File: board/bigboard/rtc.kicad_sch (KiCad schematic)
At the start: 4 parts, among them U12 PCF85263AT{slash}AJ, Y2 32.768kHz

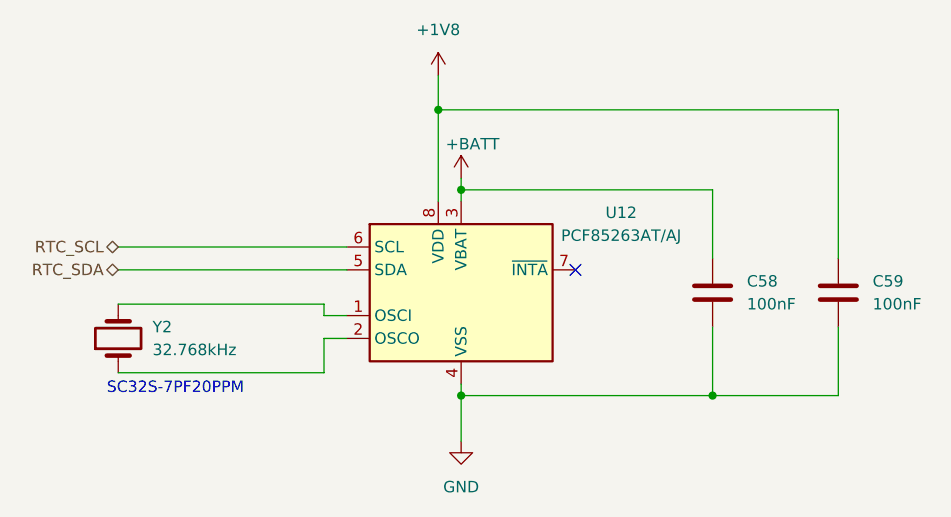
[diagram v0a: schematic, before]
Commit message: Manufactured version of bigboard
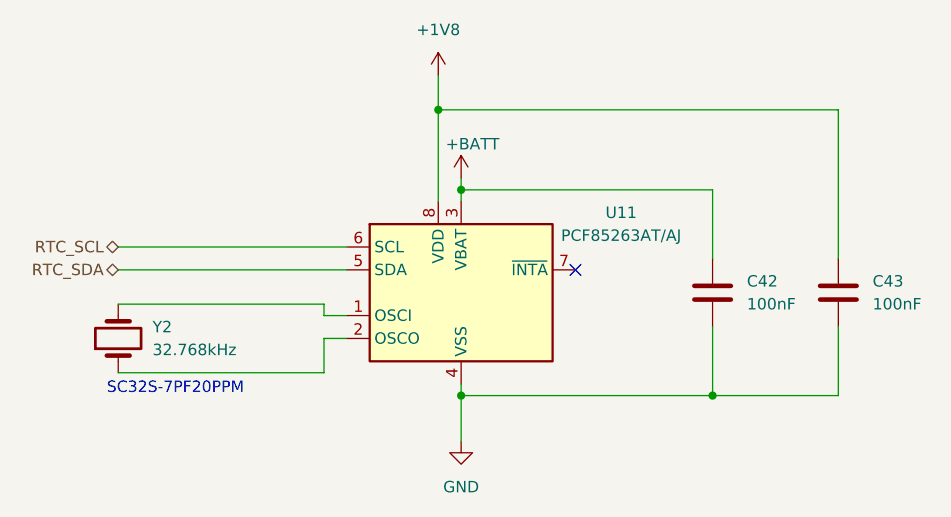
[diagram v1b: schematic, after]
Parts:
- C42: renamed from C58; MPN (none) -> CC0201KRX5R8BB104
- C43: renamed from C59; MPN (none) -> CC0201KRX5R8BB104
- renumbered U12 to U11
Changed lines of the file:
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@@
   (symbol (lib_id "Device:C") (at 176.53 99.06 0) (unit 1)
     (in_bom yes) (on_board yes) (fields_autoplaced)
-    (property "Reference" "C59" (id 0) (at 180.34 97.7899 0)
+    (property "Reference" "C43" (id 0) (at 180.34 97.7899 0)
       (effects (font (size 1.27 1.27)) (justify left))
     )
@@
       (effects (font (size 1.27 1.27)) hide)
     )
+    (property "MPN" "CC0201KRX5R8BB104" (id 5) (at 176.53 99.06 0)
+      (effects (font (size 1.27 1.27)) hide)
+    )
     (pin "1")
     (pin "2")
@@
   (symbol (lib_id "power:GND") (at 134.62 115.57 0) (unit 1)
     (in_bom yes) (on_board yes) (fields_autoplaced)
-    (property "Reference" "#PWR055" (id 0) (at 134.62 121.92 0)
+    (property "Reference" "#PWR051" (id 0) (at 134.62 121.92 0)
       (effects (font (size 1.27 1.27)) hide)
     )
@@
   (symbol (lib_id "Device:C") (at 162.56 99.06 0) (unit 1)
     (in_bom yes) (on_board yes) (fields_autoplaced)
-    (property "Reference" "C58" (id 0) (at 166.37 97.7899 0)
+    (property "Reference" "C42" (id 0) (at 166.37 97.7899 0)
       (effects (font (size 1.27 1.27)) (justify left))
     )
@@
       (effects (font (size 1.27 1.27)) hide)
     )
+    (property "MPN" "CC0201KRX5R8BB104" (id 5) (at 162.56 99.06 0)
+      (effects (font (size 1.27 1.27)) hide)
+    )
     (pin "1")
     (pin "2")
@@
   (symbol (lib_id "Timer_RTC:PCF85263AT") (at 134.62 99.06 0) (unit 1)
     (in_bom yes) (on_board yes)
-    (property "Reference" "U12" (id 0) (at 152.4 90.17 0))
+    (property "Reference" "U11" (id 0) (at 152.4 90.17 0))
     (property "Value" "PCF85263AT{slash}AJ" (id 1) (at 152.4 92.71 0))
     (property "Footprint" "Package_SO:SOIC-8_3.9x4.9mm_P1.27mm" (id 2) (at 134.62 120.65 0)
@@
   (symbol (lib_id "power:+1V8") (at 132.08 74.93 0) (unit 1)
     (in_bom yes) (on_board yes) (fields_autoplaced)
-    (property "Reference" "#PWR053" (id 0) (at 132.08 78.74 0)
+    (property "Reference" "#PWR049" (id 0) (at 132.08 78.74 0)
       (effects (font (size 1.27 1.27)) hide)
     )
@@
   (symbol (lib_id "power:+BATT") (at 134.62 86.36 0) (unit 1)
     (in_bom yes) (on_board yes)
-    (property "Reference" "#PWR054" (id 0) (at 134.62 90.17 0)
+    (property "Reference" "#PWR050" (id 0) (at 134.62 90.17 0)
       (effects (font (size 1.27 1.27)) hide)
     )
